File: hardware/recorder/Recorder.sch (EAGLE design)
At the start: 41 parts, among them T1 ZVN4424A, T2 ZVN4424A, U1 DEV-16771_REDUCED_PINS, U2 MCP4822-E/P, U3 LM6132BIN, U4 Value, U5 L7808ABV, U6 L7908CV

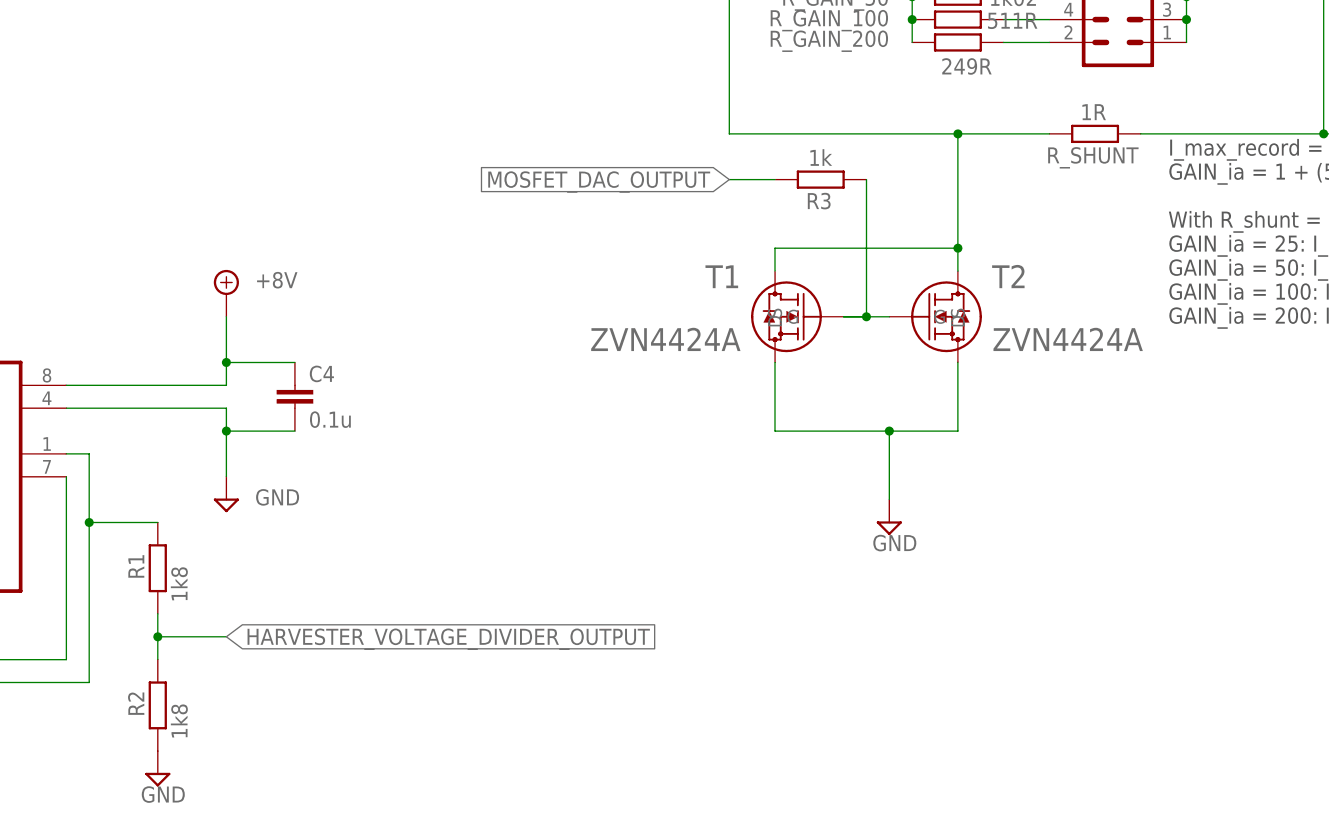
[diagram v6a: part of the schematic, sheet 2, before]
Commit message: Add new recorder MOSFET and update the existing one
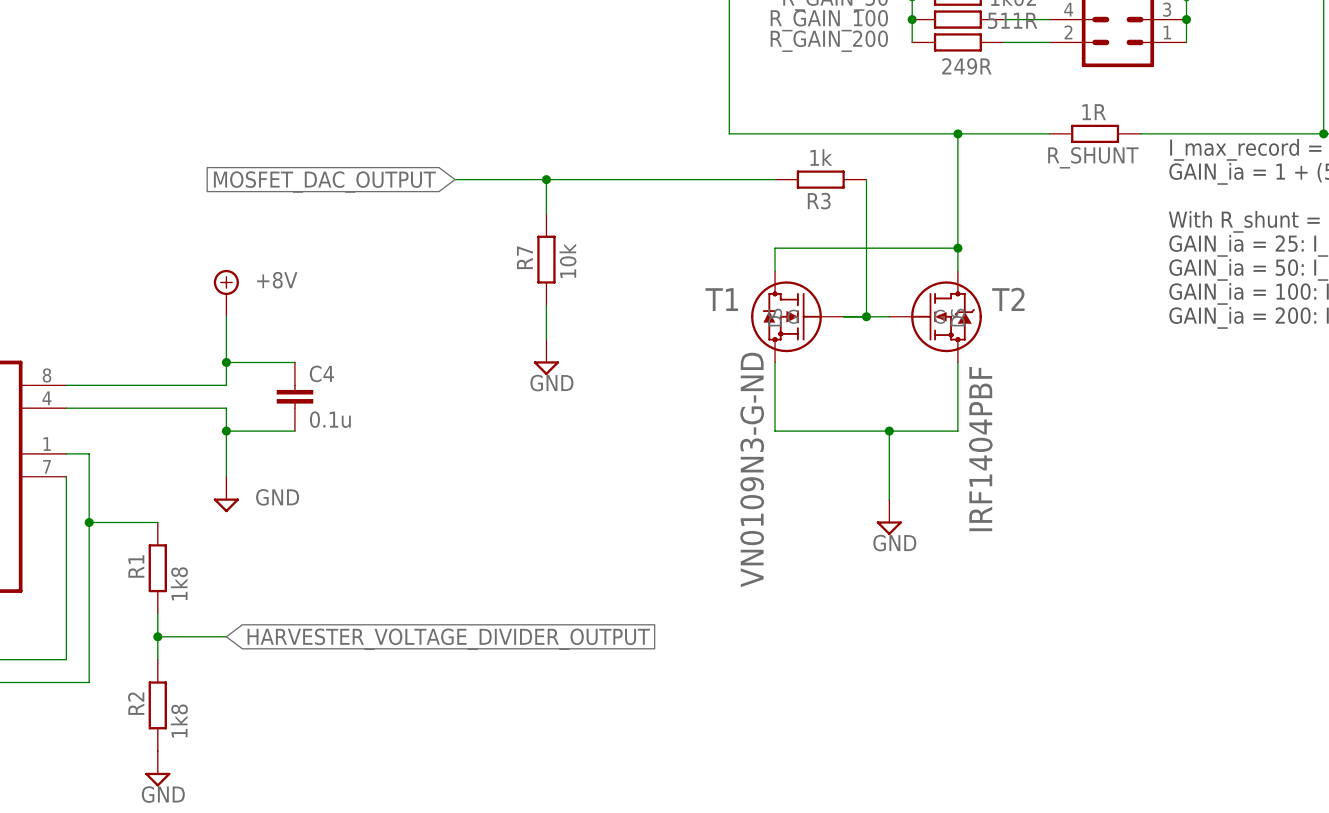
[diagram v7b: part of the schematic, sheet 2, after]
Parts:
- added R7: 10k, rcl:R-EU_0207/10
- T1: value ZVN4424A -> VN0109N3-G-ND; device NES_Solar_Cell_Recorder_And_Emulator:ZVN4424A -> NES_Solar_Cell_Recorder_And_Emulator:VN0109N3-G-ND
- T2: value ZVN4424A -> IRF1404PBF; device NES_Solar_Cell_Recorder_And_Emulator:ZVN4424A -> IRF1404PBF:IRF1404PBF
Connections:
- net GND: now also R7.1
- net MOSFET_DAC_OUTPUT: now also R7.2
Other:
- note added: "v0.3.11"
- note removed: "v0.2.6"
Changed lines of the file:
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@@
 <part name="SUPPLY20" library="supply2" library_urn="urn:adsk.eagle:library:372" deviceset="GND" device=""/>
 <part name="U4" library="INA121PA" deviceset="INA121PA" device="" value="Value"/>
-<part name="T2" library="NES_Solar_Cell_Recorder_And_Emulator" deviceset="ZVN4424A" device=""/>
 <part name="R_SHUNT" library="rcl" library_urn="urn:adsk.eagle:library:334" deviceset="R-EU_" device="0207/10" package3d_urn="urn:adsk.eagle:package:23491/2" value="1R"/>
 <part name="R_GAIN_25" library="rcl" library_urn="urn:adsk.eagle:library:334" deviceset="R-EU_" device="0207/10" package3d_urn="urn:adsk.eagle:package:23491/2" value="2k1"/>
@@
 <part name="C13" library="rcl" library_urn="urn:adsk.eagle:library:334" deviceset="C-EU" device="025-024X044" package3d_urn="urn:adsk.eagle:package:23630/1" value="1u"/>
 <part name="C4" library="rcl" library_urn="urn:adsk.eagle:library:334" deviceset="C-EU" device="025-024X044" package3d_urn="urn:adsk.eagle:package:23630/1" value="0.1u"/>
-<part name="T1" library="NES_Solar_Cell_Recorder_And_Emulator" deviceset="ZVN4424A" device=""/>
+<part name="T1" library="NES_Solar_Cell_Recorder_And_Emulator" deviceset="VN0109N3-G-ND" device=""/>
 <part name="D1" library="diode" library_urn="urn:adsk.eagle:library:210" deviceset="1N581*" device="" package3d_urn="urn:adsk.eagle:package:43421/1" technology="7-B"/>
 <part name="+3V1" library="supply1" library_urn="urn:adsk.eagle:library:371" deviceset="+3V3" device=""/>
@@
 <part name="R6" library="rcl" library_urn="urn:adsk.eagle:library:334" deviceset="R-EU_" device="0207/10" package3d_urn="urn:adsk.eagle:package:23491/2" value="330R"/>
 <part name="ERROR" library="led" library_urn="urn:adsk.eagle:library:259" deviceset="LED" device="5MM" package3d_urn="urn:adsk.eagle:package:15799/2"/>
+<part name="T2" library="IRF1404PBF" deviceset="IRF1404PBF" device=""/>
+<part name="R7" library="rcl" library_urn="urn:adsk.eagle:library:334" deviceset="R-EU_" device="0207/10" package3d_urn="urn:adsk.eagle:package:23491/2" value="10k"/>
+<part name="SUPPLY33" library="supply2" library_urn="urn:adsk.eagle:library:372" deviceset="GND" device=""/>
 </parts>
 <sheets>
@@
 <plain>
 <text x="215.9" y="20.32" size="2.54" layer="94">SOCRAETES Recorder</text>
-<text x="215.9" y="15.24" size="2.54" layer="94">v0.2.6</text>
+<text x="215.9" y="15.24" size="2.54" layer="94">v0.3.11</text>
 <text x="215.9" y="10.16" size="2.54" layer="94">Author: S.Mosavat</text>
 <text x="162.56" y="7.62" size="2.54" layer="94">University of Duisburg-Essen
@@
 <attribute name="VALUE" x="194.0814" y="131.8006" size="2.0828" layer="96" ratio="6" rot="SR90"/>
 </instance>
-<instance part="T2" gate="A" x="175.26" y="63.5" smashed="yes">
-<attribute name="NAME" x="186.69" y="66.675" size="2.54" layer="95" ratio="10" rot="SR0"/>
-<attribute name="VALUE" x="186.69" y="59.69" size="2.54" layer="96" ratio="10" rot="SR0"/>
-</instance>
 <instance part="R_SHUNT" gate="G$1" x="198.12" y="83.82" smashed="yes" rot="R180">
 <attribute name="NAME" x="202.946" y="82.3214" size="1.778" layer="95" rot="R180"/>
@@
 </instance>
 <instance part="T1" gate="A" x="170.18" y="63.5" smashed="yes" rot="MR0">
-<attribute name="NAME" x="158.75" y="66.675" size="2.54" layer="95" ratio="10" rot="SMR0"/>
-<attribute name="VALUE" x="158.75" y="59.69" size="2.54" layer="96" ratio="10" rot="SMR0"/>
+<attribute name="NAME" x="158.75" y="64.135" size="2.54" layer="95" ratio="10" rot="SMR0"/>
+<attribute name="VALUE" x="161.29" y="59.69" size="2.54" layer="96" ratio="10" rot="SMR270"/>
 </instance>
 <instance part="R_GAIN_100" gate="G$1" x="182.88" y="96.52" smashed="yes" rot="R180">
@@
 <attribute name="NAME" x="175.26" y="99.8474" size="1.778" layer="95" rot="R180"/>
 <attribute name="VALUE" x="191.77" y="99.822" size="1.778" layer="96" rot="R180"/>
+</instance>
+<instance part="T2" gate="A" x="175.26" y="63.5" smashed="yes">
+<attribute name="NAME" x="186.69" y="64.135" size="2.54" layer="95" ratio="10" rot="SR0"/>
+<attribute name="VALUE" x="186.69" y="39.37" size="2.54" layer="96" ratio="10" rot="SR90"/>
+</instance>
+<instance part="R7" gate="G$1" x="137.16" y="69.85" smashed="yes" rot="R90">
+<attribute name="NAME" x="135.6614" y="68.58" size="1.778" layer="95" rot="R90"/>
+<attribute name="VALUE" x="140.462" y="67.564" size="1.778" layer="96" rot="R90"/>
+</instance>
+<instance part="SUPPLY33" gate="GND" x="137.16" y="58.42" smashed="yes">
+<attribute name="VALUE" x="135.255" y="55.245" size="1.778" layer="96"/>
 </instance>
 </instances>
@@
 <pinref part="T1" gate="A" pin="S"/>
 <wire x1="162.56" y1="58.42" x2="162.56" y2="50.8" width="0.1524" layer="91"/>
-<pinref part="T2" gate="A" pin="S"/>
 <wire x1="162.56" y1="50.8" x2="175.26" y2="50.8" width="0.1524" layer="91"/>
 <wire x1="175.26" y1="50.8" x2="182.88" y2="50.8" width="0.1524" layer="91"/>
@@
 <wire x1="175.26" y1="43.18" x2="175.26" y2="50.8" width="0.1524" layer="91"/>
 <junction x="175.26" y="50.8"/>
+<pinref part="T2" gate="A" pin="S"/>
+</segment>
+<segment>
+<pinref part="SUPPLY33" gate="GND" pin="GND"/>
+<pinref part="R7" gate="G$1" pin="1"/>
+<wire x1="137.16" y1="60.96" x2="137.16" y2="64.77" width="0.1524" layer="91"/>
 </segment>
 </net>
@@
 <net name="N$6" class="0">
 <segment>
-<pinref part="T2" gate="A" pin="D"/>
 <pinref part="U4" gate="A" pin="IN-"/>
 <wire x1="157.48" y1="83.82" x2="157.48" y2="111.76" width="0.1524" layer="91"/>
@@
 <wire x1="182.88" y1="83.82" x2="193.04" y2="83.82" width="0.1524" layer="91"/>
 <junction x="182.88" y="83.82"/>
+<pinref part="T2" gate="A" pin="D"/>
 </segment>
 </net>
@@
 <segment>
 <pinref part="R3" gate="G$1" pin="2"/>
-<wire x1="162.56" y1="78.74" x2="157.48" y2="78.74" width="0.1524" layer="91"/>
-<label x="157.48" y="78.74" size="1.778" layer="95" rot="R180" xref="yes"/>
+<wire x1="162.56" y1="78.74" x2="137.16" y2="78.74" width="0.1524" layer="91"/>
+<label x="127" y="78.74" size="1.778" layer="95" rot="R180" xref="yes"/>
+<wire x1="137.16" y1="78.74" x2="127" y2="78.74" width="0.1524" layer="91"/>
+<pinref part="R7" gate="G$1" pin="2"/>
+<wire x1="137.16" y1="74.93" x2="137.16" y2="78.74" width="0.1524" layer="91"/>
+<junction x="137.16" y="78.74"/>
 </segment>
 <segment>
@@
 <net name="N$11" class="0">
 <segment>
-<pinref part="T2" gate="A" pin="G"/>
 <pinref part="R3" gate="G$1" pin="1"/>
 <wire x1="172.72" y1="78.74" x2="172.72" y2="63.5" width="0.1524" layer="91"/>
@@
 <junction x="172.72" y="63.5"/>
 <wire x1="170.18" y1="63.5" x2="175.26" y2="63.5" width="0.1524" layer="91"/>
-</segment>
-</net>
+<pinref part="T2" gate="A" pin="G"/>
+</segment>
+</net>

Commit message: Add minor changes to the hardware
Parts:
- R_SHUNT: value 1R -> 2R
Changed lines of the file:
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@@
 <part name="SUPPLY20" library="supply2" library_urn="urn:adsk.eagle:library:372" deviceset="GND" device=""/>
 <part name="U4" library="INA121PA" deviceset="INA121PA" device="" value="Value"/>
-<part name="R_SHUNT" library="rcl" library_urn="urn:adsk.eagle:library:334" deviceset="R-EU_" device="0207/10" package3d_urn="urn:adsk.eagle:package:23491/2" value="1R"/>
+<part name="R_SHUNT" library="rcl" library_urn="urn:adsk.eagle:library:334" deviceset="R-EU_" device="0207/10" package3d_urn="urn:adsk.eagle:package:23491/2" value="2R"/>
 <part name="R_GAIN_25" library="rcl" library_urn="urn:adsk.eagle:library:334" deviceset="R-EU_" device="0207/10" package3d_urn="urn:adsk.eagle:package:23491/2" value="2k1"/>
 <part name="SUPPLY8" library="supply2" library_urn="urn:adsk.eagle:library:372" deviceset="GND" device=""/>
